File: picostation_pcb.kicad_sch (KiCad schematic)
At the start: 13 parts, among them J1 Conn_01x06_Female, J2 Conn_01x20_Female, J3 PICO, J4 Conn_01x20_Female, U1 LM78M05_TO252

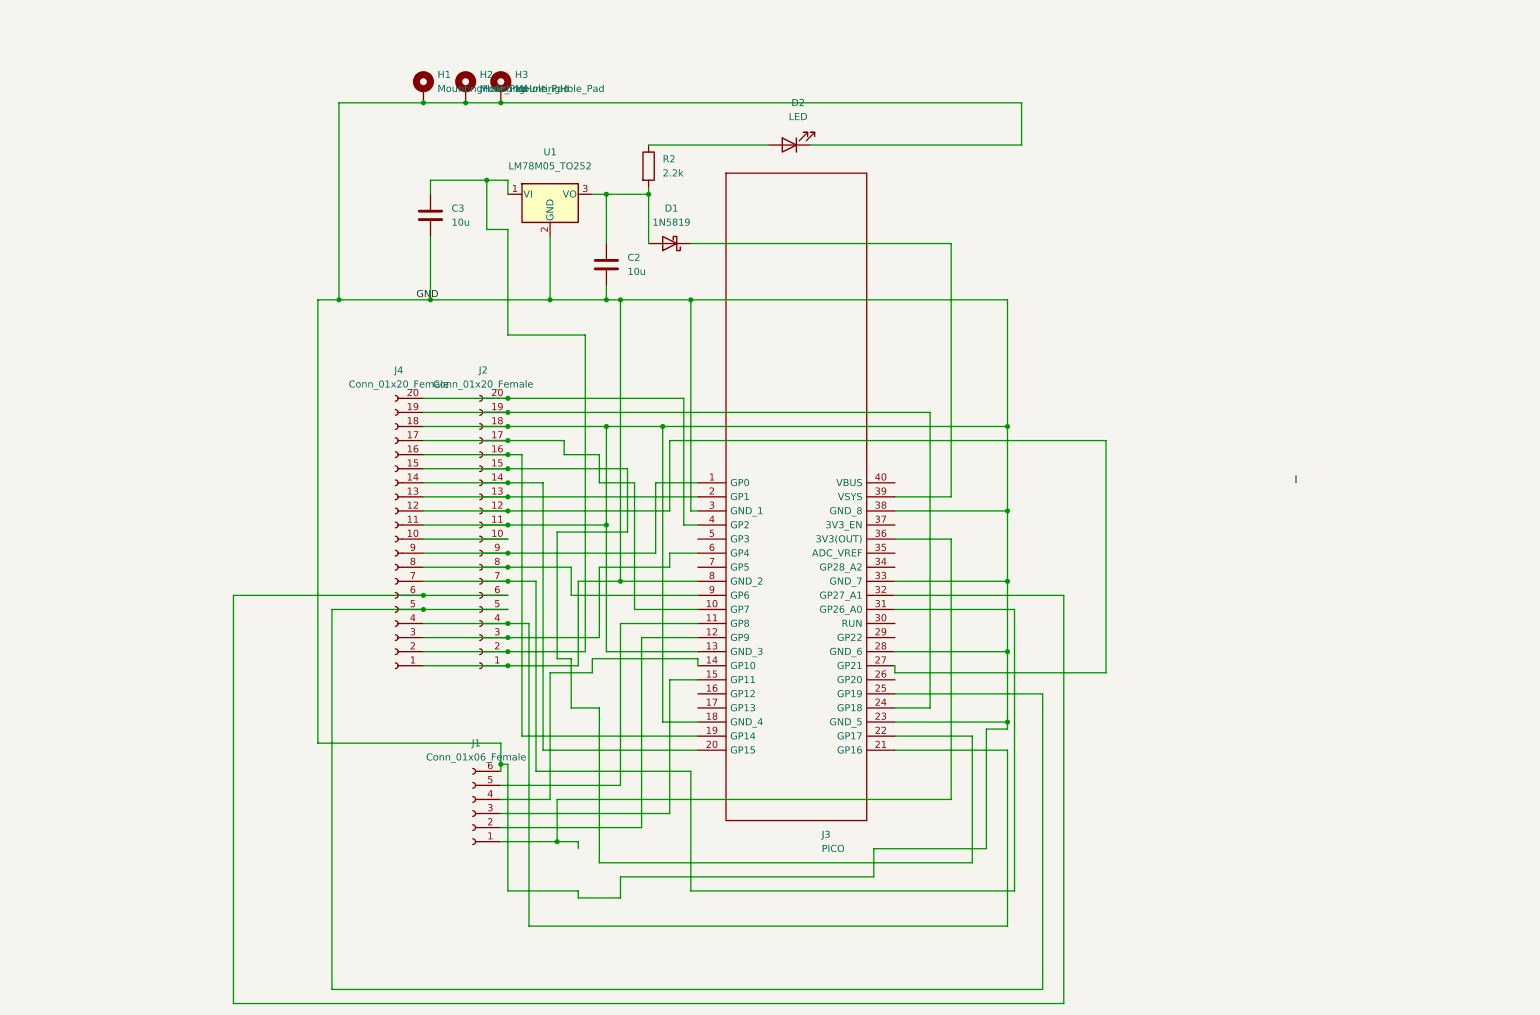
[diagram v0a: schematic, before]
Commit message: Tidied up Sch by using labels
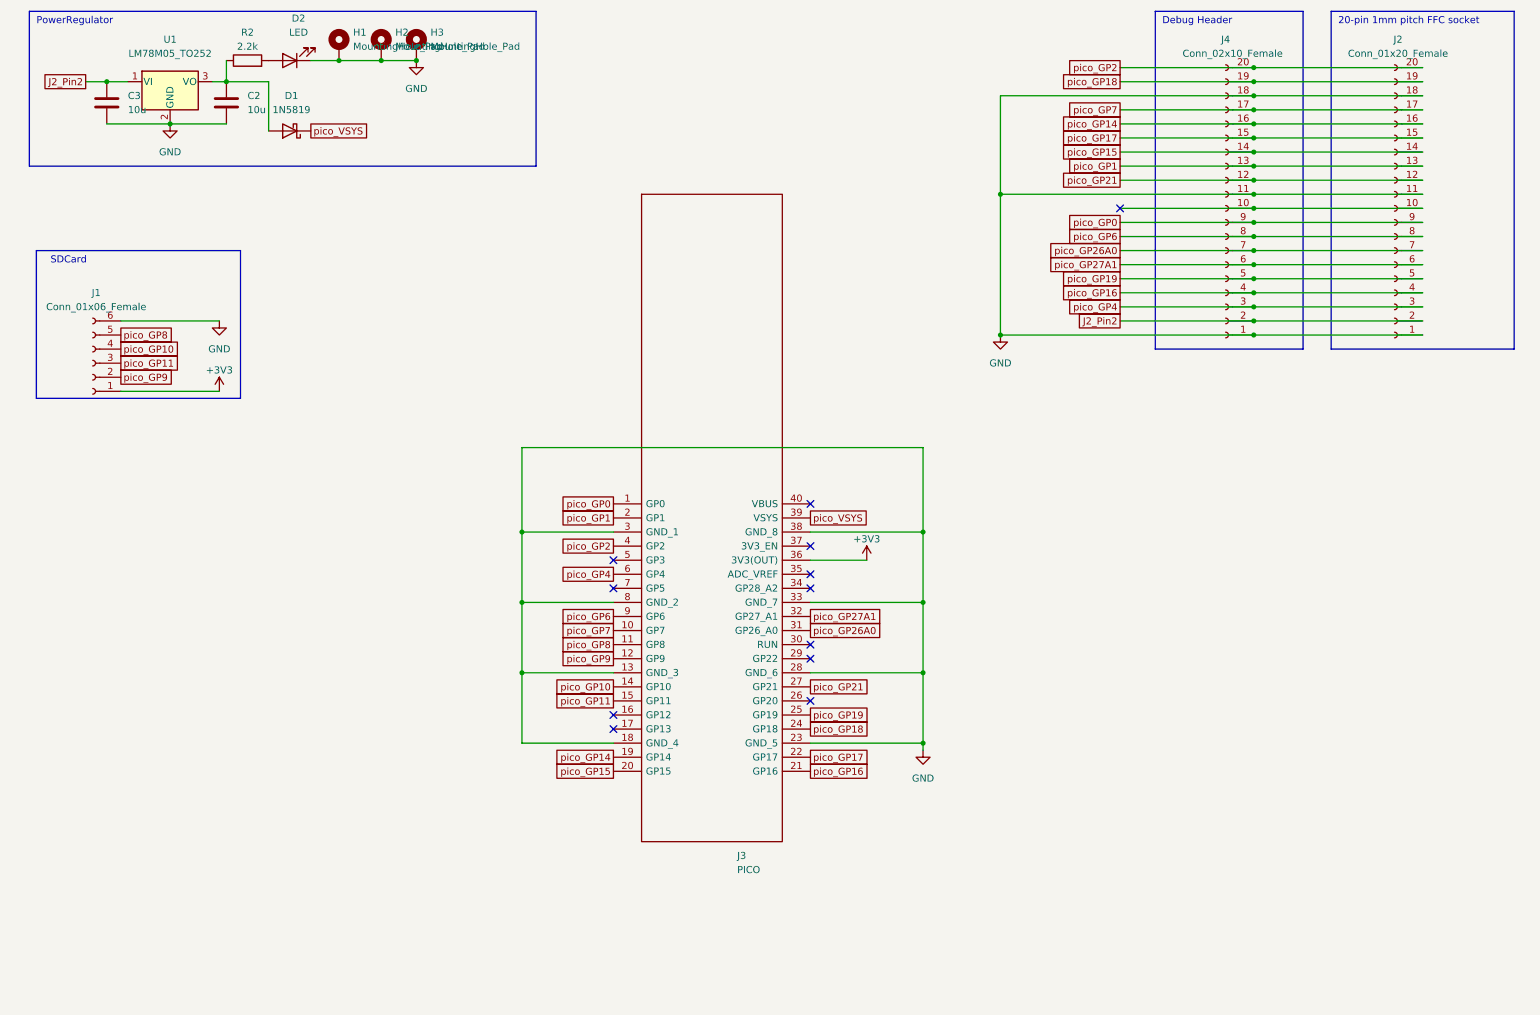
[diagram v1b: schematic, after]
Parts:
- J4: value Conn_01x20_Female -> Conn_02x10_Female
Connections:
- net at C2.1, D1.2 (A), U1.3 (VO): now also R2.1; no longer R2.2
- net pico_VSYS: now reaches D1.1 (K), J3.39 (VSYS)
- net at D2.2 (A): now also R2.2; no longer R2.1
- net pico_GP21: now reaches J2.12 (Pin_12), J3.27 (GP21), J4.12 (Pin_12)
- net pico_GP1: now reaches J2.13 (Pin_13), J3.2 (GP1), J4.13 (Pin_13)
- net pico_GP15: now reaches J2.14 (Pin_14), J3.20 (GP15), J4.14 (Pin_14)
- net pico_GP17: now reaches J2.15 (Pin_15), J3.22 (GP17), J4.15 (Pin_15)
- net pico_GP14: now reaches J2.16 (Pin_16), J3.19 (GP14), J4.16 (Pin_16)
- net pico_GP7: now reaches J2.17 (Pin_17), J3.10 (GP7), J4.17 (Pin_17)
- net pico_GP18: now reaches J2.19 (Pin_19), J3.24 (GP18), J4.19 (Pin_19)
- net J2_Pin2: now reaches C3.1, J2.2 (Pin_2), J4.2 (Pin_2), U1.1 (VI)
- net pico_GP2: now reaches J2.20 (Pin_20), J3.4 (GP2), J4.20 (Pin_20)
- net pico_GP4: now reaches J2.3 (Pin_3), J3.6 (GP4), J4.3 (Pin_3)
- net pico_GP16: now reaches J2.4 (Pin_4), J3.21 (GP16), J4.4 (Pin_4)
- net pico_GP19: now reaches J2.5 (Pin_5), J3.25 (GP19), J4.5 (Pin_5)
- net pico_GP27A1: now reaches J2.6 (Pin_6), J3.32 (GP27_A1), J4.6 (Pin_6)
- net pico_GP26A0: now reaches J2.7 (Pin_7), J3.31 (GP26_A0), J4.7 (Pin_7)
- net pico_GP6: now reaches J2.8 (Pin_8), J3.9 (GP6), J4.8 (Pin_8)
- net pico_GP0: now reaches J2.9 (Pin_9), J3.1 (GP0), J4.9 (Pin_9)
- net pico_GP8: now reaches J1.5 (Pin_5), J3.11 (GP8)
- net pico_GP9: now reaches J1.2 (Pin_2), J3.12 (GP9)
- net pico_GP10: now reaches J1.4 (Pin_4), J3.14 (GP10)
- net pico_GP11: now reaches J1.3 (Pin_3), J3.15 (GP11)
- net +3V3: now reaches J1.1 (Pin_1), J3.36 (3V3(OUT))
- no-connect marks 0 -> 12
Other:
- note added: "20-pin 1mm pitch FFC socket"
- note added: "Debug Header"
- note added: "PowerRegulator"
- note added: "SDCard"
- moved on the sheet: C2, C3, D1, D2, H1, H2, H3, J1, J2, J3, J4, R2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

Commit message: Updated References
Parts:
- renumbered C3 to C1, R2 to R1
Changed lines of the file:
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@@
   (symbol (lib_id "Device:R") (at 53.34 22.86 90) (unit 1)
     (in_bom yes) (on_board yes) (dnp no) (fields_autoplaced)
-    (property "Reference" "R2" (at 53.34 17.78 90)
+    (property "Reference" "R1" (at 53.34 17.78 90)
       (effects (font (size 1.27 1.27)))
     )
@@
       (project "picostation_pcb"
         (path "/69032557-405f-457b-8a9a-4ca4fb07928c"
-          (reference "R2") (unit 1)
+          (reference "R1") (unit 1)
         )
       )
@@
   (symbol (lib_id "Device:C") (at 27.94 30.48 0) (unit 1)
     (in_bom yes) (on_board yes) (dnp no) (fields_autoplaced)
-    (property "Reference" "C3" (at 31.75 29.2099 0)
+    (property "Reference" "C1" (at 31.75 29.845 0)
       (effects (font (size 1.27 1.27)) (justify left))
     )
-    (property "Value" "10u" (at 31.75 31.7499 0)
+    (property "Value" "10u" (at 31.75 32.385 0)
       (effects (font (size 1.27 1.27)) (justify left))
     )
@@
       (project "picostation_pcb"
         (path "/69032557-405f-457b-8a9a-4ca4fb07928c"
-          (reference "C3") (unit 1)
+          (reference "C1") (unit 1)
         )
       )

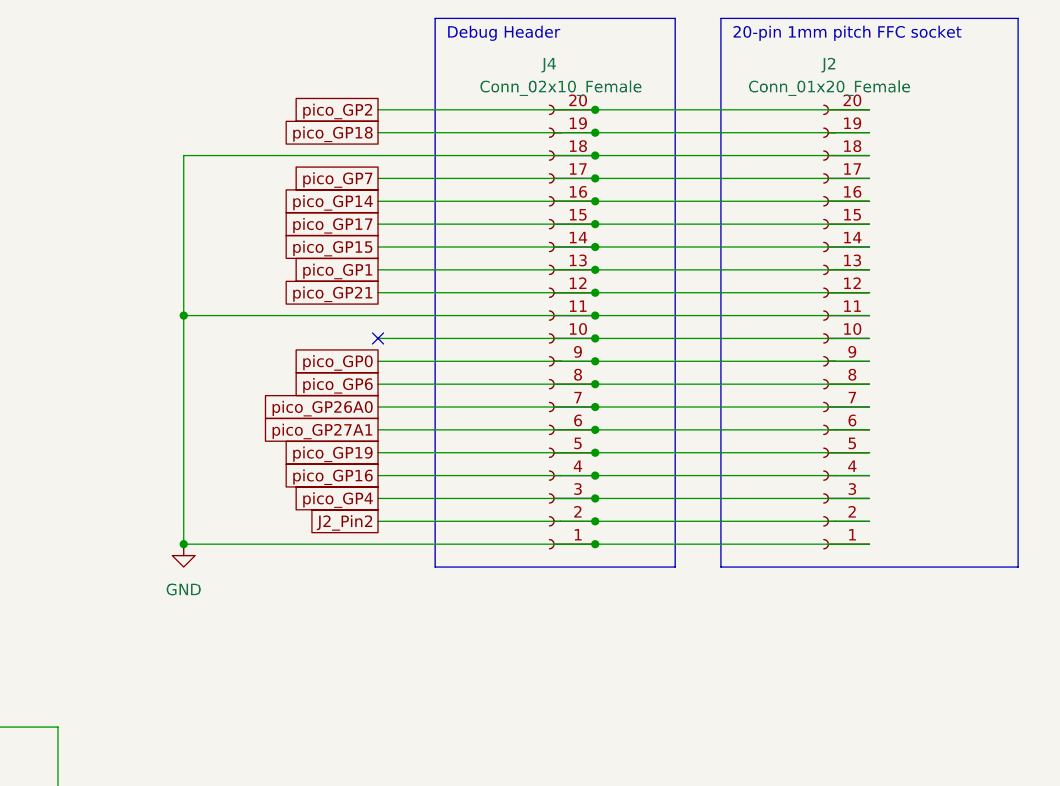
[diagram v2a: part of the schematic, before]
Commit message: Change J4 to 02x10 in Sch
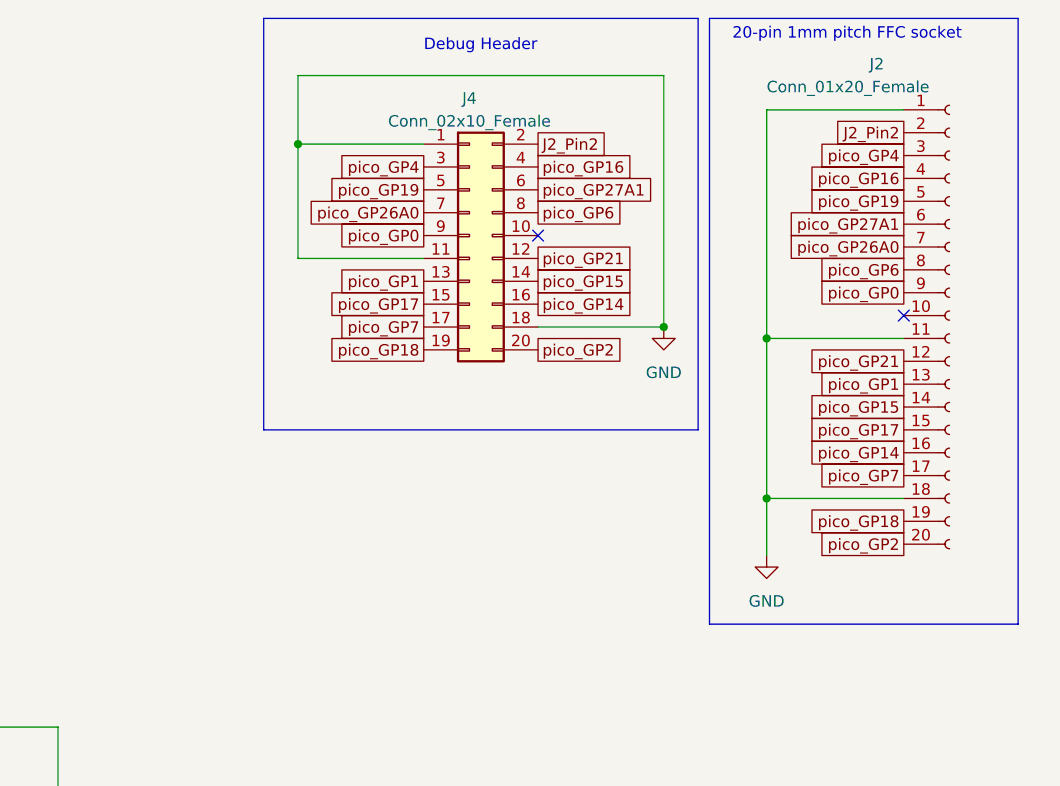
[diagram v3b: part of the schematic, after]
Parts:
- J4: symbol Connector:Conn_01x20_Female -> Connector_Generic:Conn_02x10_Odd_Even
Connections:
- net at J4.10 (Pin_10): no longer J2.10 (Pin_10)
- no-connect marks 12 -> 13
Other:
- moved on the sheet: J2

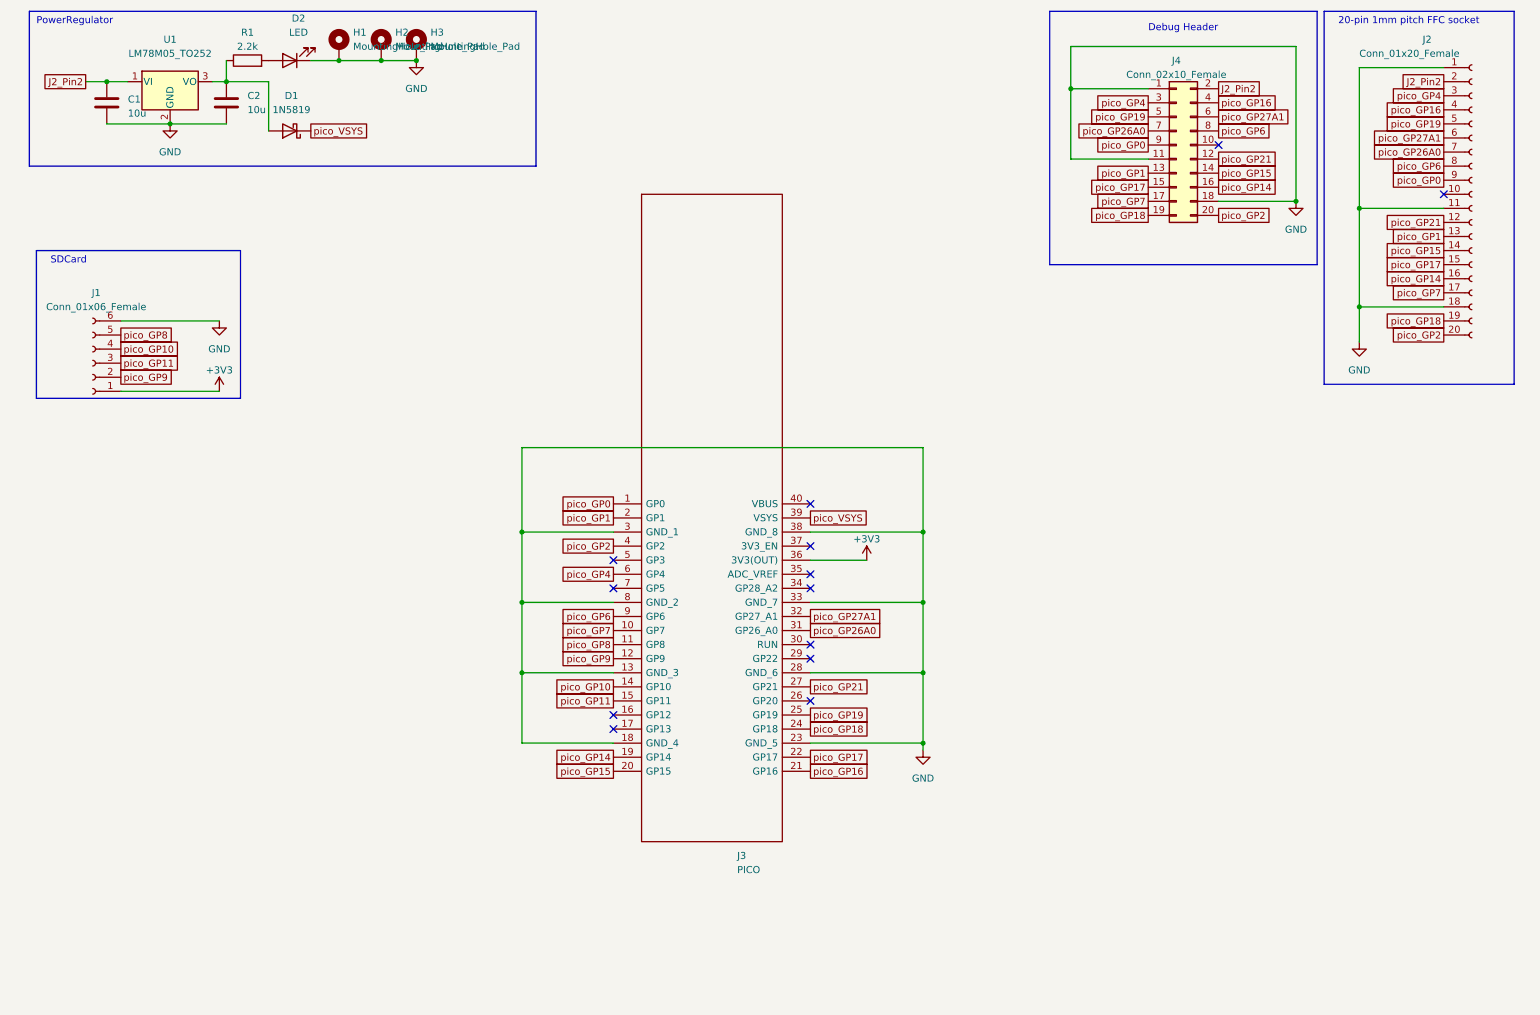
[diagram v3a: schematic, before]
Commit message: Updated Global NETs to use Proper PSX Connection point names
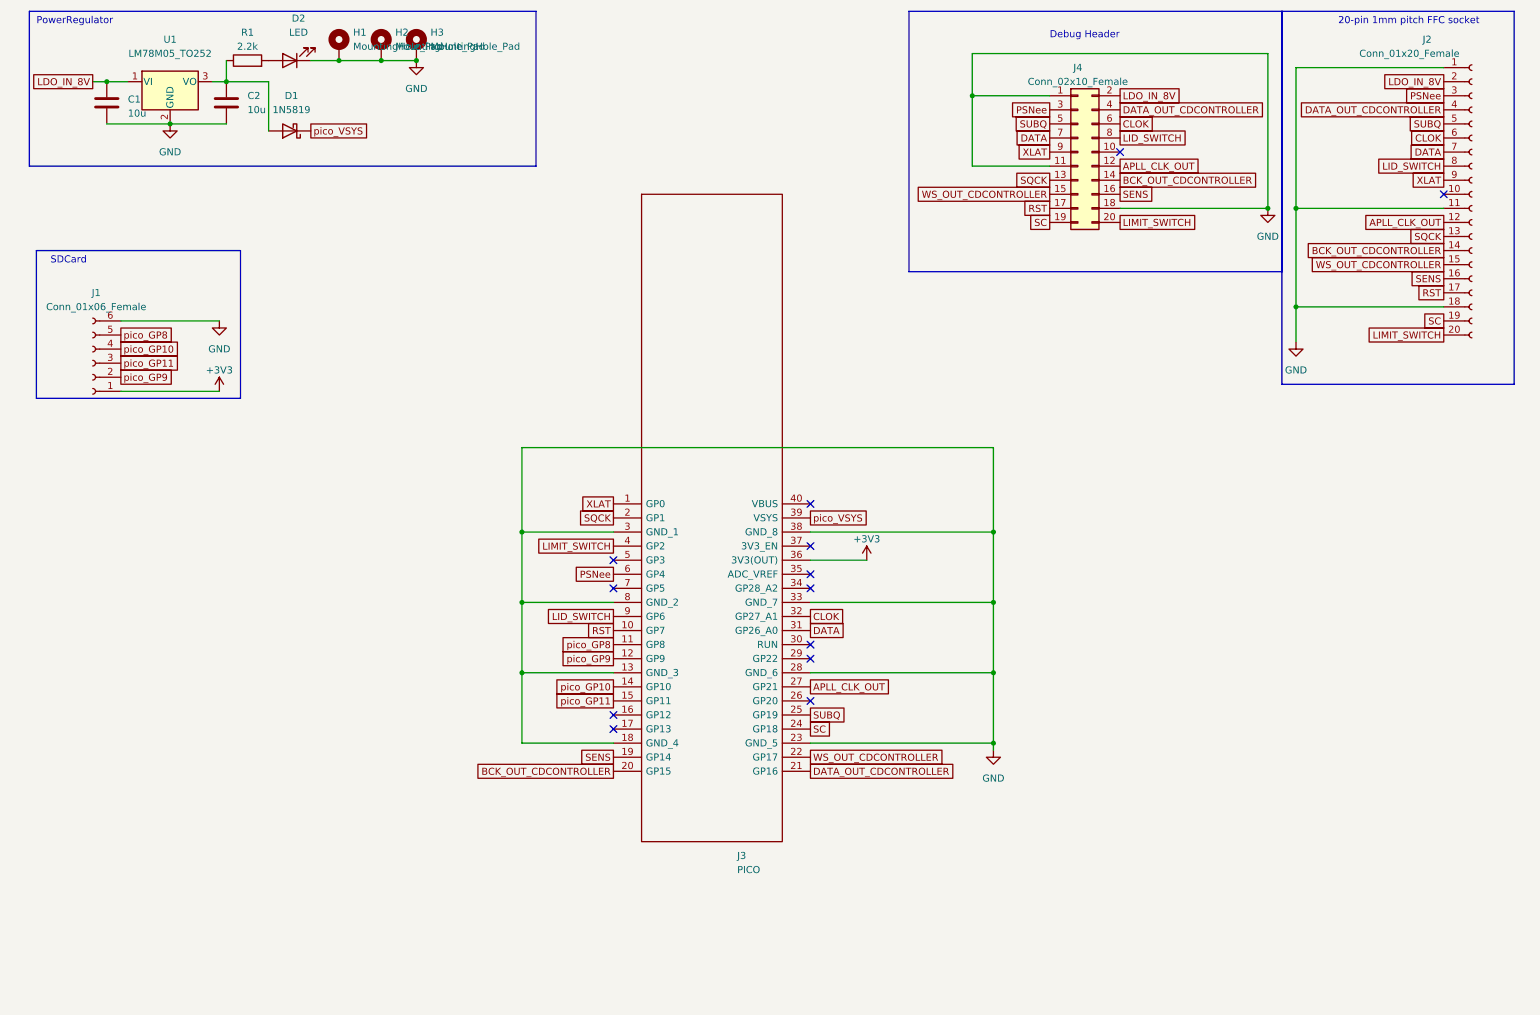
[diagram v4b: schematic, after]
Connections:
- net J2_Pin2 renamed LDO_IN_8V
- net pico_GP0 renamed XLAT
- net pico_GP1 renamed SQCK
- net pico_GP14 renamed SENS
- net pico_GP15 renamed BCK_OUT_CDCONTROLLER
- net pico_GP16 renamed DATA_OUT_CDCONTROLLER
- net pico_GP17 renamed WS_OUT_CDCONTROLLER
- net pico_GP18 renamed SC
- net pico_GP19 renamed SUBQ
- net pico_GP2 renamed LIMIT_SWITCH
- net pico_GP21 renamed APLL_CLK_OUT
- net pico_GP26A0 renamed DATA
- net pico_GP27A1 renamed CLOK
- net pico_GP4 renamed PSNee
- net pico_GP6 renamed LID_SWITCH
- net pico_GP7 renamed RST
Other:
- moved on the sheet: J4
